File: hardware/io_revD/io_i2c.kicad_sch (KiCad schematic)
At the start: 54 parts, among them J1 Target Interface, 2716 Pinout, J10 Conn_01x01, J11 Conn_01x01, J12 Conn_01x01, J13 Conn_01x01, J14 Conn_01x01, J15 Conn_01x01, J2 Jumper Block, J3 Jumper Block, J4 Target Interface, 2716 Pinout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

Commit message: Remove C6, Updated warning label, new pdf
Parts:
- removed C6: 0.1uF, Capacitor_SMD:C_0603_1608Metric, symbol Device:C
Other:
- note added: "unhook from target when programming"
- note removed: "unhook from target and unhook i2c jumpers when programming"
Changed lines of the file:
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@@
     (title "Demon Debugger ROM-IO Interface - I2C Version")
     (date "2022-02-27")
-    (rev "C")
+    (rev "D")
   )
   (junction (at 180.975 220.98) (diameter 0) (color 0 0 0 0)
@@
     (stroke (width 0) (type default) (color 0 0 0 0))
   )
-  (wire (pts (xy 292.1 33.655) (xy 292.1 34.925))
-    (stroke (width 0) (type default) (color 0 0 0 0))
-  )
   (wire (pts (xy 213.36 83.185) (xy 209.55 83.185))
     (stroke (width 0) (type default) (color 0 0 0 0))
@@
     (stroke (width 0) (type default) (color 0 0 0 0))
   )
-  (wire (pts (xy 292.1 42.545) (xy 292.1 43.815))
-    (stroke (width 0) (type default) (color 0 0 0 0))
-  )
   (wire (pts (xy 257.81 32.385) (xy 257.81 33.655))
     (stroke (width 0) (type default) (color 0 0 0 0))
@@
     (effects (font (size 1.27 1.27)) (justify left bottom))
   )
-  (text "unhook from target and unhook i2c jumpers when programming"
-    (at 247.015 116.84 0)
+  (text "unhook from target when programming" (at 256.54 116.84 0)
     (effects (font (size 1.27 1.27)) (justify left bottom))
   )
@@
   )
   (label "A10" (at 294.64 83.185 0)
-    (effects (font (size 1.27 1.27)) (justify left bottom))
-  )
-  (label "program WR" (at 292.1 33.655 90)
     (effects (font (size 1.27 1.27)) (justify left bottom))
   )
@@
     (pin "1")
   )
-  (symbol (lib_id "power:GND") (at 292.1 43.815 0) (unit 1)
-    (in_bom yes) (on_board yes)
-    (property "Reference" "#PWR0124" (id 0) (at 292.1 50.165 0)
-      (effects (font (size 1.27 1.27)) hide)
-    )
-    (property "Value" "GND" (id 1) (at 292.227 48.2092 0))
-    (property "Footprint" "" (id 2) (at 292.1 43.815 0)
-      (effects (font (size 1.27 1.27)) hide)
-    )
-    (property "Datasheet" "" (id 3) (at 292.1 43.815 0)
-      (effects (font (size 1.27 1.27)) hide)
-    )
-    (pin "1")
-  )
   (symbol (lib_id "74xx:74LS125") (at 43.815 76.2 0) (unit 2)
     (in_bom yes) (on_board yes)
@@
     (pin "2")
   )
-  (symbol (lib_id "Device:C") (at 292.1 38.735 0) (unit 1)
-    (in_bom yes) (on_board yes)
-    (property "Reference" "C6" (id 0) (at 295.021 37.5666 0)
-      (effects (font (size 1.27 1.27)) (justify left))
-    )
-    (property "Value" "0.1uF" (id 1) (at 295.021 39.878 0)
-      (effects (font (size 1.27 1.27)) (justify left))
-    )
-    (property "Footprint" "Capacitor_SMD:C_0603_1608Metric" (id 2) (at 293.0652 42.545 0)
-      (effects (font (size 1.27 1.27)) hide)
-    )
-    (property "Datasheet" "~" (id 3) (at 292.1 38.735 0)
-      (effects (font (size 1.27 1.27)) hide)
-    )
-    (pin "1")
-    (pin "2")
-  )
   (symbol (lib_id "power:+5VD") (at 79.375 131.445 0) (mirror y) (unit 1)
     (in_bom yes) (on_board yes) (fields_autoplaced)
@@
       (reference "#PWR0123") (unit 1) (value "+5V") (footprint "")
     )
-    (path "/1aa68458-e219-4589-b1da-318e232d7e2d"
-      (reference "#PWR0124") (unit 1) (value "GND") (footprint "")
-    )
     (path "/00000000-0000-0000-0000-000061057968"
       (reference "#PWR0125") (unit 1) (value "GND") (footprint "")
@@
       (reference "C5") (unit 1) (value "0.1uF") (footprint "Capacitor_THT:C_Axial_L3.8mm_D2.6mm_P7.50mm_Horizontal")
     )
-    (path "/efa4de96-1b8d-4c26-9986-2d2b7c98ddb6"
-      (reference "C6") (unit 1) (value "0.1uF") (footprint "Capacitor_SMD:C_0603_1608Metric")
-    )
     (path "/ed6cafba-b430-499a-9a09-3ac50b37c7cf"

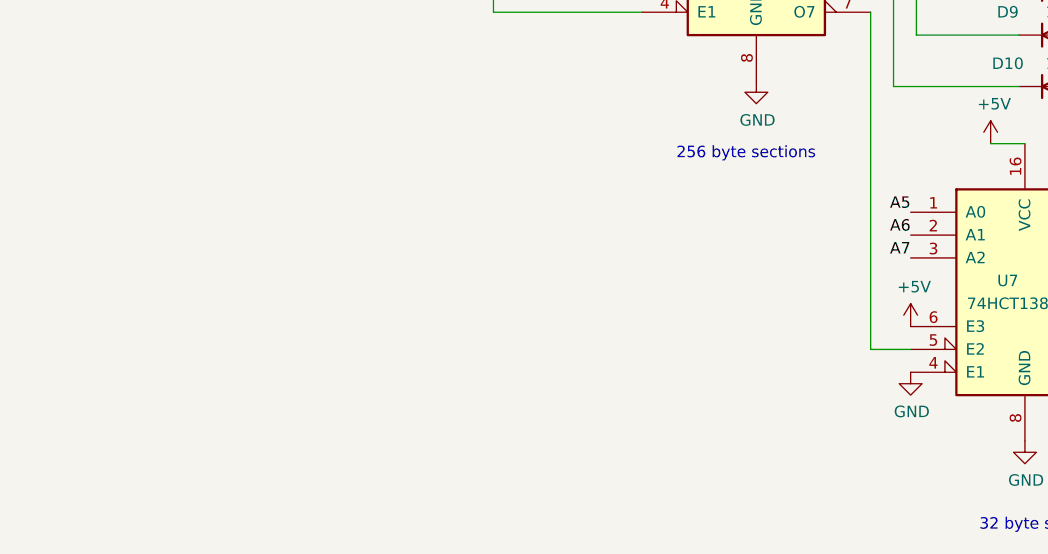
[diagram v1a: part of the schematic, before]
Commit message: New msg about shorter roms
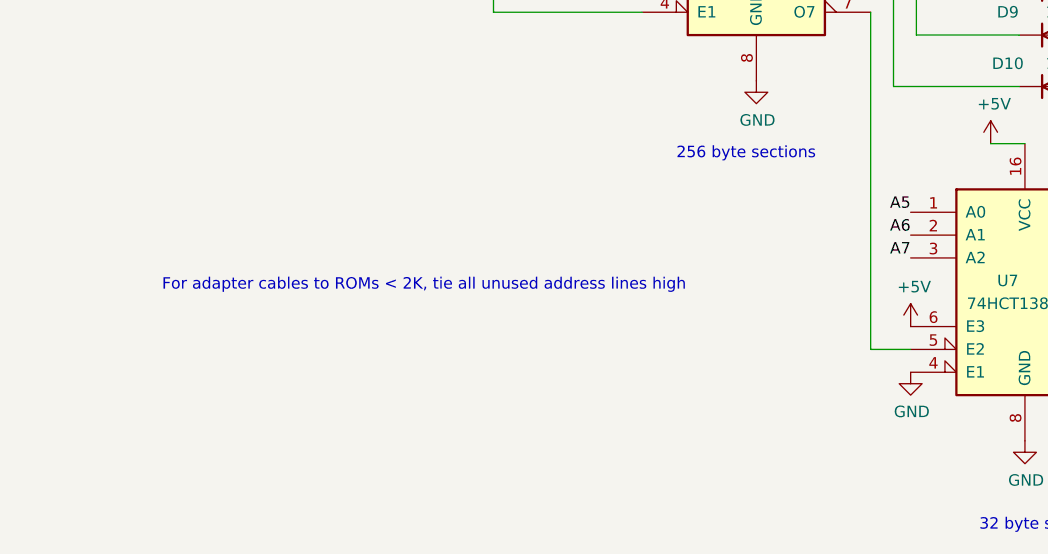
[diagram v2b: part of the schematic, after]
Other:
- note added: "For adapter cables to ROMs < 2K, tie all unused address lines high"
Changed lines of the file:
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@@
+    (effects (font (size 1.27 1.27)) (justify left bottom))
+  )
+  (text "For adapter cables to ROMs < 2K, tie all unused address lines high"
+    (at 43.18 224.79 0)
     (effects (font (size 1.27 1.27)) (justify left bottom))
   )

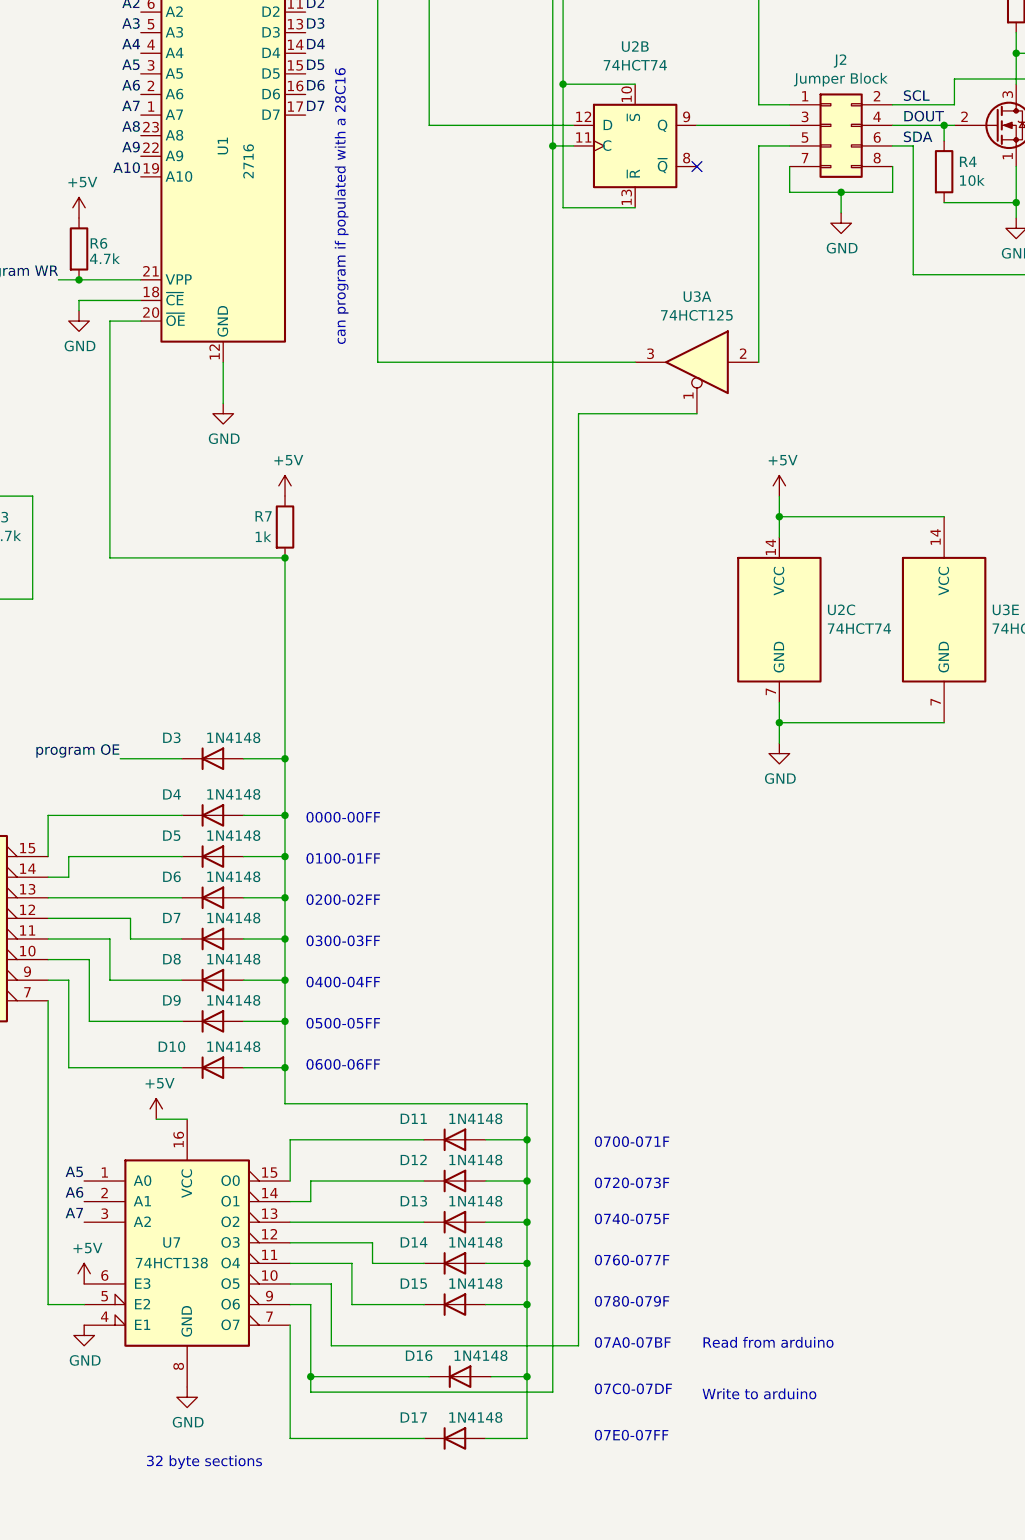
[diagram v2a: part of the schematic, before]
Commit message: added silk regions, labeling, jumper for rom emulator mode
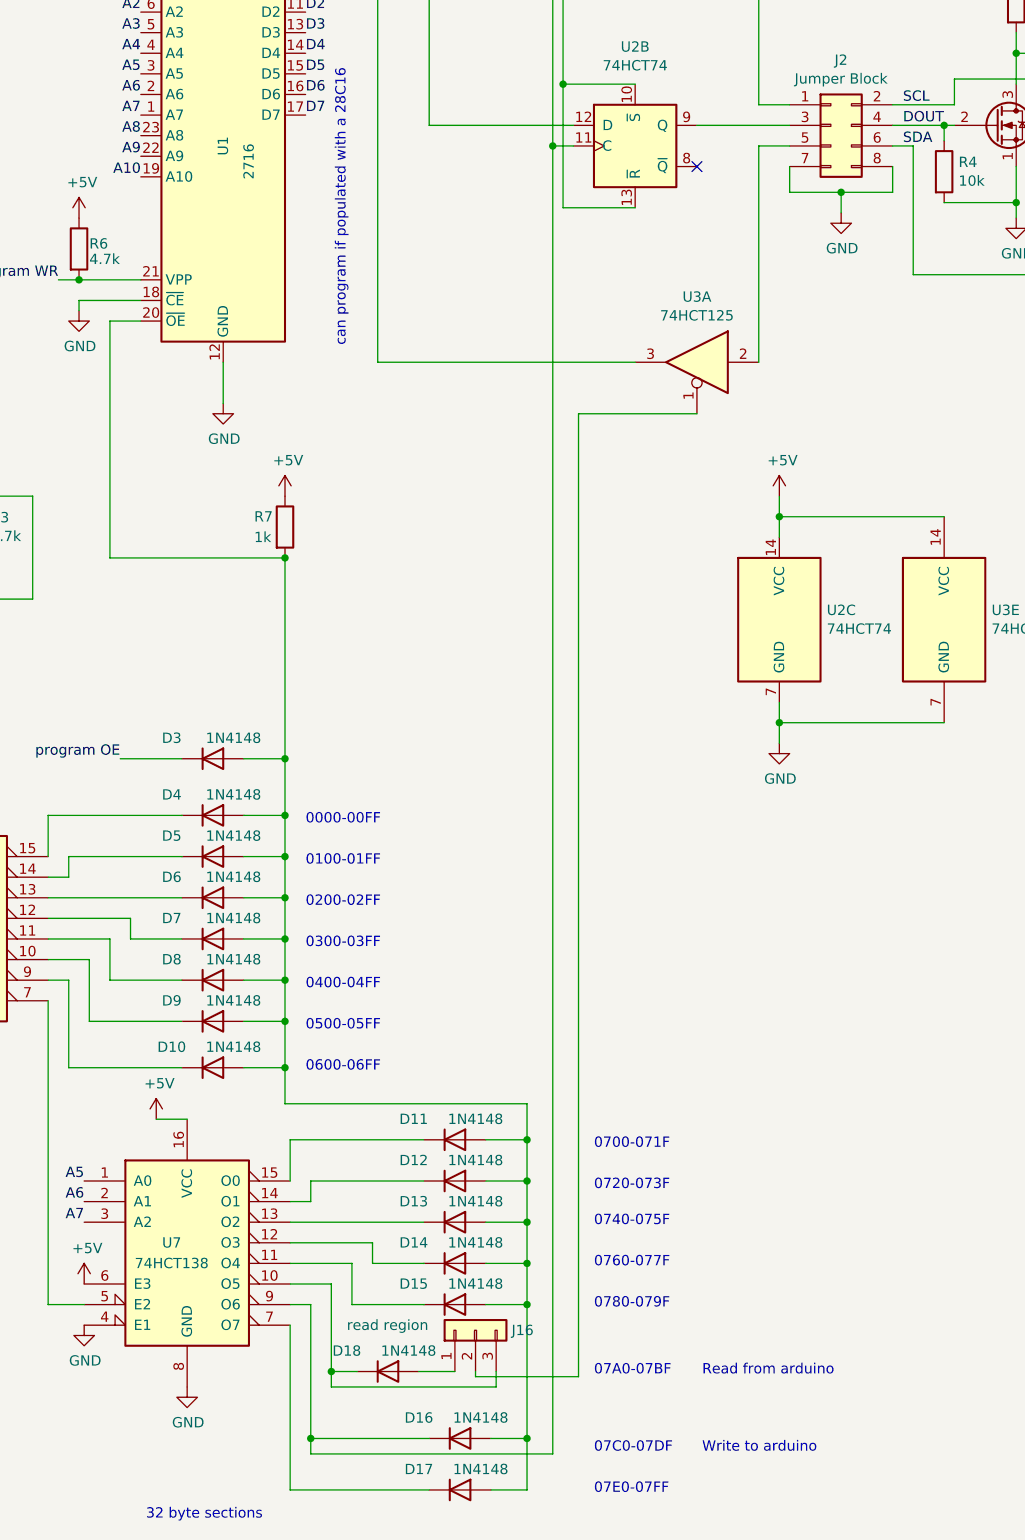
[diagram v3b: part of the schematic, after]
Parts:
- added D18: 1N4148, Diode_THT:D_DO-35_SOD27_P2.54mm_Vertical_AnodeUp, symbol Diode:1N4148
- added J16: read region, Connector_PinHeader_2.54mm:PinHeader_1x03_P2.54mm_Vertical, symbol Connector_Generic:Conn_01x03
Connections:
- net at U3.1: now also J16.2 (Pin_2); no longer U7.10 (O5)
- new net: D18.2 (A), J16.1 (Pin_1)
- new net: D18.1 (K), J16.3 (Pin_3), U7.10 (O5)
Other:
- moved on the sheet: D16, D17

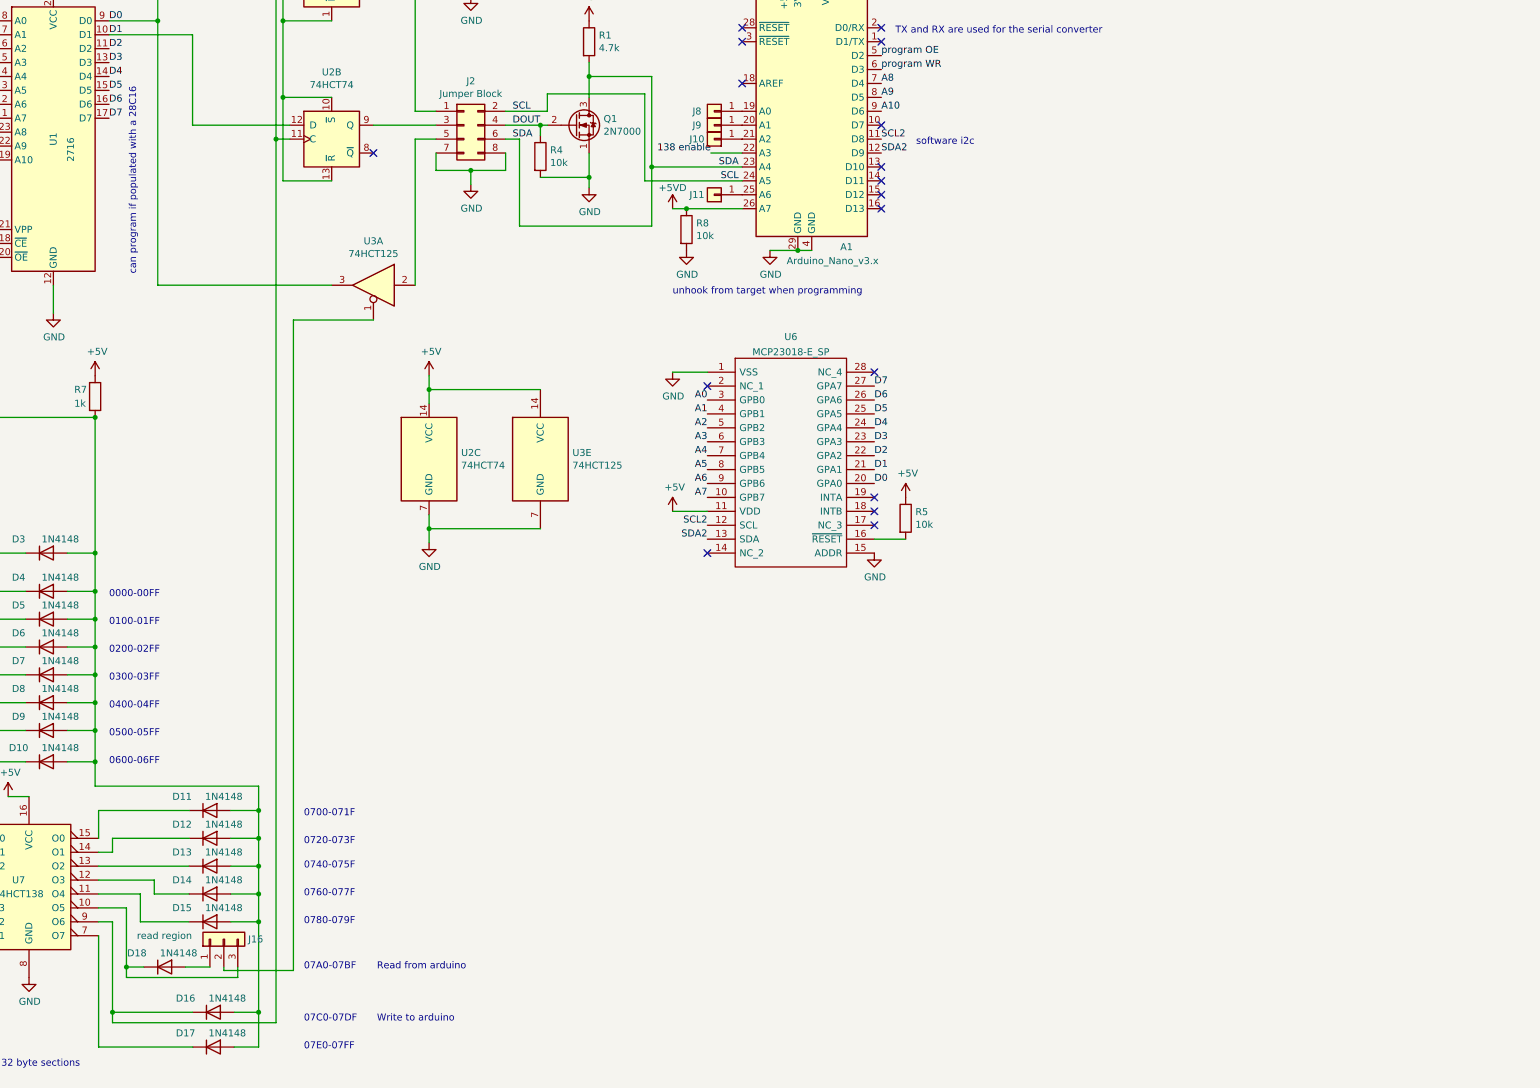
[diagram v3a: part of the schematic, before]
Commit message: fixed silk, locations, and jumper
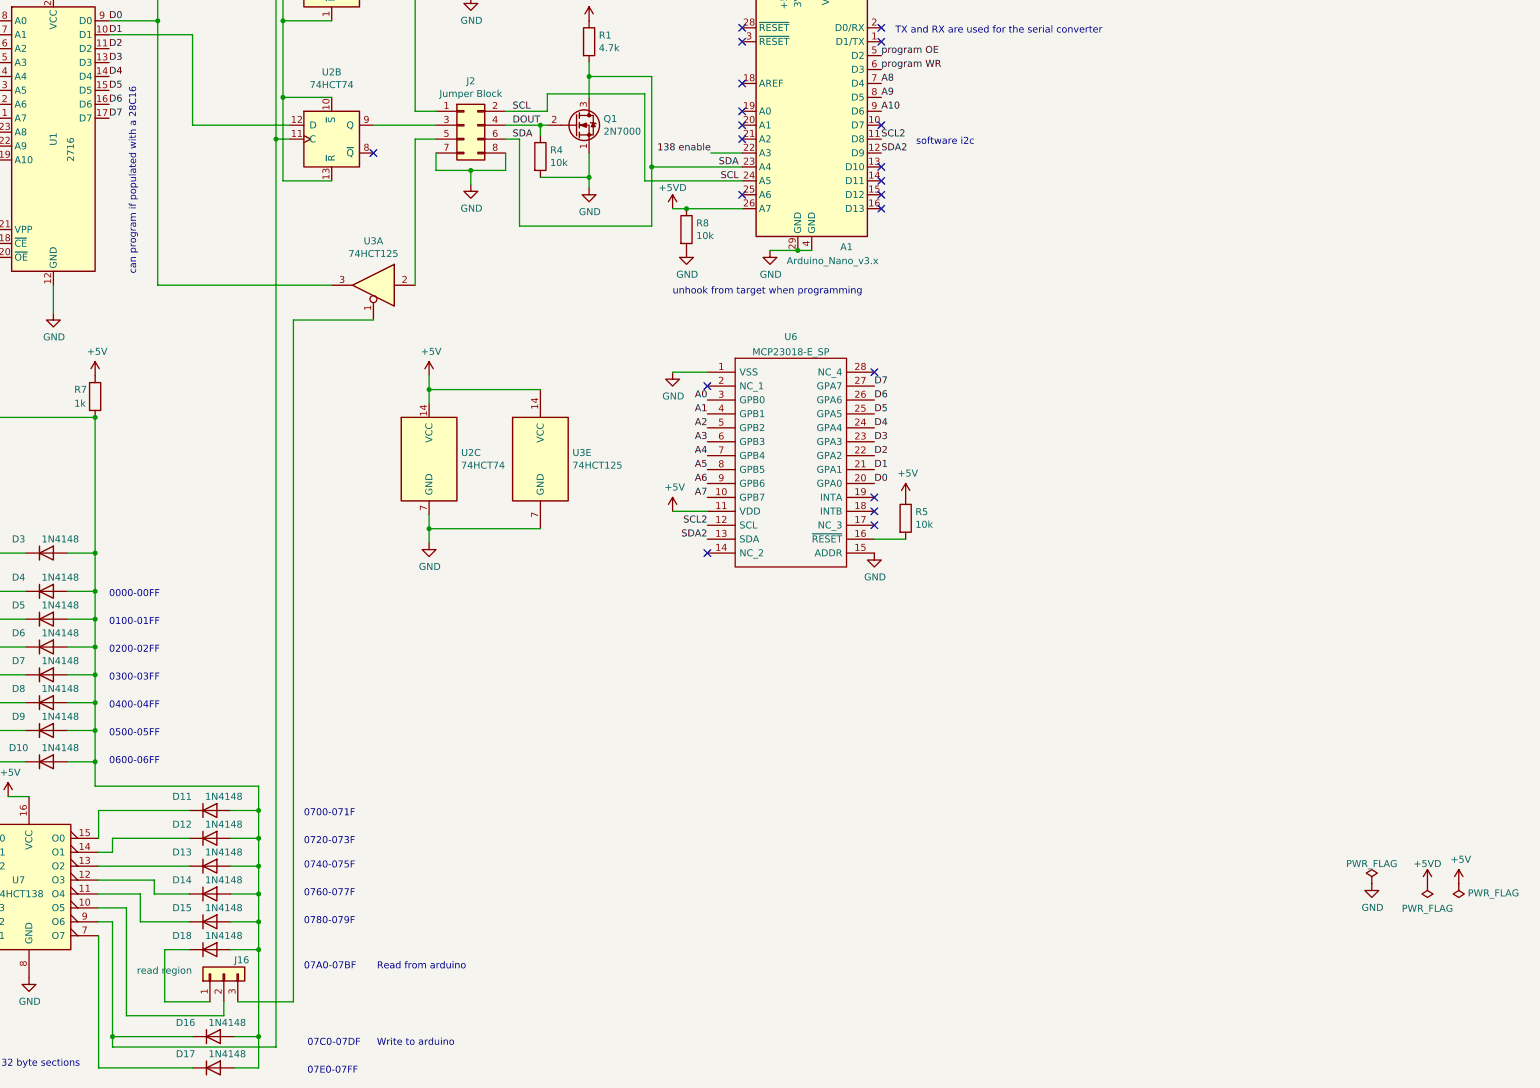
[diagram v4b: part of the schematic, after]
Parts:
- removed J10, J11, J8, J9: Conn_01x01, Connector_PinHeader_2.54mm:PinHeader_1x01_P2.54mm_Vertical, symbol Connector_Generic:Conn_01x01
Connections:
- net at D10.2 (A), D11.2 (A), D12.2 (A)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: now also D18.2 (A)
- net at U3.1: now also J16.3 (Pin_3); no longer J16.2 (Pin_2)
- net at J16.1 (Pin_1): now also D18.1 (K); no longer D18.2 (A)
- new net: J16.2 (Pin_2), U7.10 (O5)
- no-connect marks 22 -> 26
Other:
- moved on the sheet: D16, D17, D18, J16

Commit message: Update schematic symbols from pcb
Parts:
- D10, D11, D12, D13, D14, D15, D16, D17, D18, D3, D4, D5, D6, D7, D8, D9: footprint Diode_THT:D_DO-35_SOD27_P2.54mm_Vertical_AnodeUp -> Diode_THT:D_DO-35_SOD27_P2.54mm_Vertical_KathodeUp
- Q1: footprint Package_TO_SOT_THT:TO-92_Inline -> Package_TO_SOT_THT:TO-92_Wide
